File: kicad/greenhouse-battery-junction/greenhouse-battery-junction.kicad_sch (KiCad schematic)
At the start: 8 parts, among them J1 Conn_01x10_Female, J10 Conn_01x03_Female, J11 Screw_Terminal_01x02, J12 Conn_01x04_Male, J13 Screw_Terminal_01x02, J2 Conn_01x03_Female

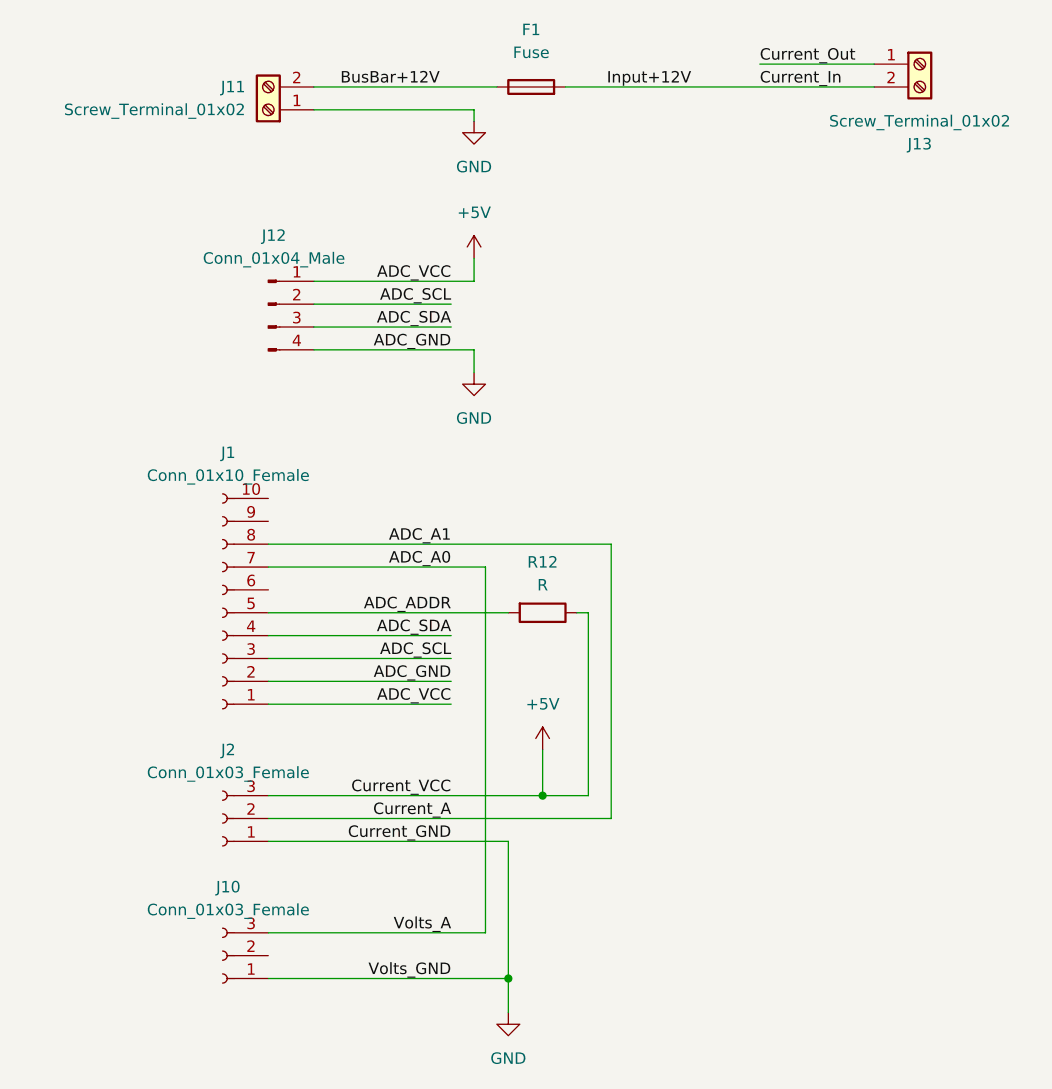
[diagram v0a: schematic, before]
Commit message: Fixed errors in battery junction
Didn't match up with prototype
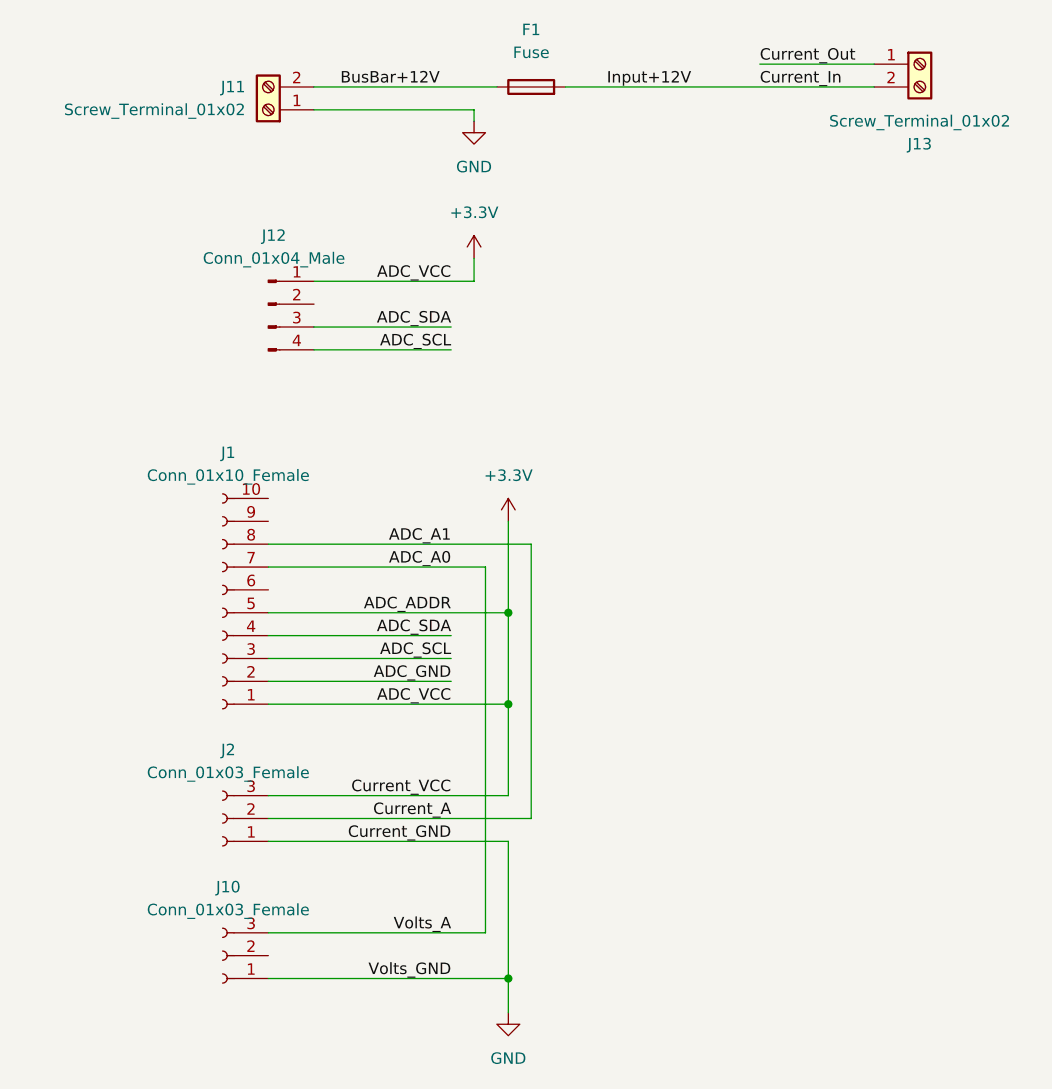
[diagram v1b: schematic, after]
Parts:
- removed R12: R, Resistor_THT:R_Box_L8.4mm_W2.5mm_P5.08mm, symbol Device:R
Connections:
- net ADC_ADDR is gone; now on net +3V3: J1.5 (Pin_5)
- net ADC_SCL: now also J12.4 (Pin_4); no longer J12.2 (Pin_2)
- net GND: no longer J1.2 (Pin_2), J12.4 (Pin_4)
- net +5V renamed +3V3
- new net ADC_GND: J1.2 (Pin_2)
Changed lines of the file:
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@@
 (kicad_sch (version 20211123) (generator eeschema)
   (paper "A4")
+  (junction (at 82.55 93.98) (diameter 0) (color 0 0 0 0)
+  )
+  (junction (at 82.55 104.14) (diameter 0) (color 0 0 0 0)
+  )
   (junction (at 82.55 134.62) (diameter 0) (color 0 0 0 0)
   )
-  (junction (at 86.36 114.3) (diameter 0) (color 0 0 0 0)
+  (wire (pts (xy 60.96 62.23) (xy 76.2 62.23))
+    (stroke (width 0) (type default) (color 0 0 0 0))
   )
   (wire (pts (xy 82.55 134.62) (xy 82.55 138.43))
     (stroke (width 0) (type default) (color 0 0 0 0))
   )
-  (wire (pts (xy 55.88 114.3) (xy 86.36 114.3))
-    (stroke (width 0) (type default) (color 0 0 0 0))
-  )
-  (wire (pts (xy 91.44 93.98) (xy 91.44 114.3))
-    (stroke (width 0) (type default) (color 0 0 0 0))
-  )
-  (wire (pts (xy 60.96 62.23) (xy 76.2 62.23))
-    (stroke (width 0) (type default) (color 0 0 0 0))
-  )
-  (wire (pts (xy 60.96 59.69) (xy 76.2 59.69))
+  (wire (pts (xy 55.88 114.3) (xy 82.55 114.3))
     (stroke (width 0) (type default) (color 0 0 0 0))
   )
@@
     (stroke (width 0) (type default) (color 0 0 0 0))
   )
+  (wire (pts (xy 82.55 93.98) (xy 82.55 104.14))
+    (stroke (width 0) (type default) (color 0 0 0 0))
+  )
   (wire (pts (xy 55.88 119.38) (xy 82.55 119.38))
     (stroke (width 0) (type default) (color 0 0 0 0))
   )
-  (wire (pts (xy 55.88 86.36) (xy 93.98 86.36))
+  (wire (pts (xy 60.96 64.77) (xy 76.2 64.77))
+    (stroke (width 0) (type default) (color 0 0 0 0))
+  )
+  (wire (pts (xy 55.88 86.36) (xy 85.09 86.36))
+    (stroke (width 0) (type default) (color 0 0 0 0))
+  )
+  (wire (pts (xy 82.55 104.14) (xy 82.55 114.3))
     (stroke (width 0) (type default) (color 0 0 0 0))
   )
@@
     (stroke (width 0) (type default) (color 0 0 0 0))
   )
-  (wire (pts (xy 93.98 86.36) (xy 93.98 116.84))
-    (stroke (width 0) (type default) (color 0 0 0 0))
-  )
-  (wire (pts (xy 86.36 114.3) (xy 91.44 114.3))
-    (stroke (width 0) (type default) (color 0 0 0 0))
-  )
-  (wire (pts (xy 55.88 116.84) (xy 93.98 116.84))
-    (stroke (width 0) (type default) (color 0 0 0 0))
-  )
-  (wire (pts (xy 78.74 67.31) (xy 78.74 64.77))
-    (stroke (width 0) (type default) (color 0 0 0 0))
-  )
-  (wire (pts (xy 90.17 93.98) (xy 91.44 93.98))
+  (wire (pts (xy 85.09 86.36) (xy 85.09 116.84))
+    (stroke (width 0) (type default) (color 0 0 0 0))
+  )
+  (wire (pts (xy 55.88 116.84) (xy 85.09 116.84))
+    (stroke (width 0) (type default) (color 0 0 0 0))
+  )
+  (wire (pts (xy 55.88 104.14) (xy 82.55 104.14))
     (stroke (width 0) (type default) (color 0 0 0 0))
   )
@@
     (stroke (width 0) (type default) (color 0 0 0 0))
   )
-  (wire (pts (xy 55.88 104.14) (xy 76.2 104.14))
-    (stroke (width 0) (type default) (color 0 0 0 0))
-  )
   (wire (pts (xy 80.01 88.9) (xy 80.01 129.54))
     (stroke (width 0) (type default) (color 0 0 0 0))
@@
     (stroke (width 0) (type default) (color 0 0 0 0))
   )
-  (wire (pts (xy 86.36 109.22) (xy 86.36 114.3))
-    (stroke (width 0) (type default) (color 0 0 0 0))
-  )
   (wire (pts (xy 82.55 134.62) (xy 82.55 119.38))
     (stroke (width 0) (type default) (color 0 0 0 0))
@@
     (stroke (width 0) (type default) (color 0 0 0 0))
   )
-  (wire (pts (xy 60.96 64.77) (xy 78.74 64.77))
-    (stroke (width 0) (type default) (color 0 0 0 0))
-  )
   (wire (pts (xy 55.88 88.9) (xy 80.01 88.9))
     (stroke (width 0) (type default) (color 0 0 0 0))
@@
     (stroke (width 0) (type default) (color 0 0 0 0))
   )
+  (wire (pts (xy 82.55 83.82) (xy 82.55 93.98))
+    (stroke (width 0) (type default) (color 0 0 0 0))
+  )
   (wire (pts (xy 88.9 35.56) (xy 123.19 35.56))
     (stroke (width 0) (type default) (color 0 0 0 0))
@@
     (effects (font (size 1.27 1.27)) (justify right bottom))
   )
-  (label "ADC_SDA" (at 76.2 62.23 180)
-    (effects (font (size 1.27 1.27)) (justify right bottom))
-  )
   (label "Current_GND" (at 76.2 119.38 180)
     (effects (font (size 1.27 1.27)) (justify right bottom))
@@
     (effects (font (size 1.27 1.27)) (justify right bottom))
   )
+  (label "ADC_SCL" (at 76.2 64.77 180)
+    (effects (font (size 1.27 1.27)) (justify right bottom))
+  )
   (label "ADC_A1" (at 76.2 86.36 180)
     (effects (font (size 1.27 1.27)) (justify right bottom))
   )
   (label "ADC_VCC" (at 76.2 104.14 180)
-    (effects (font (size 1.27 1.27)) (justify right bottom))
-  )
-  (label "ADC_GND" (at 76.2 64.77 180)
     (effects (font (size 1.27 1.27)) (justify right bottom))
   )
@@
     (effects (font (size 1.27 1.27)) (justify left bottom))
   )
+  (label "ADC_SDA" (at 76.2 62.23 180)
+    (effects (font (size 1.27 1.27)) (justify right bottom))
+  )
   (label "Current_A" (at 76.2 116.84 180)
     (effects (font (size 1.27 1.27)) (justify right bottom))
@@
     (effects (font (size 1.27 1.27)) (justify right bottom))
   )
-  (label "ADC_SCL" (at 76.2 59.69 180)
-    (effects (font (size 1.27 1.27)) (justify right bottom))
-  )
   (label "ADC_VCC" (at 76.2 57.15 180)
     (effects (font (size 1.27 1.27)) (justify right bottom))
-  )
-  (symbol (lib_id "Device:R") (at 86.36 93.98 270) (unit 1)
-    (in_bom yes) (on_board yes) (fields_autoplaced)
-    (property "Reference" "R12" (id 0) (at 86.36 87.63 90)
-      (effects (font (size 1.27 1.27)) (justify top))
-    )
-    (property "Value" "R" (id 1) (at 86.36 90.17 90)
-      (effects (font (size 1.27 1.27)) (justify top))
-    )
-    (property "Footprint" "Resistor_THT:R_Box_L8.4mm_W2.5mm_P5.08mm" (id 2) (at 86.36 92.202 90)
-      (effects (font (size 1.27 1.27)) hide)
-    )
-    (property "Datasheet" "~" (id 3) (at 86.36 93.98 0)
-      (effects (font (size 1.27 1.27)) hide)
-    )
-    (pin "1")
-    (pin "2")
   )
   (symbol (lib_id "power:GND") (at 82.55 138.43 0) (unit 1)
@@
     (pin "2")
   )
-  (symbol (lib_id "power:+5V") (at 86.36 109.22 0) (unit 1)
-    (in_bom yes) (on_board yes) (fields_autoplaced)
-    (property "Reference" "#PWR0133" (id 0) (at 86.36 113.03 0)
-      (effects (font (size 1.27 1.27)) hide)
-    )
-    (property "Value" "+5V" (id 1) (at 86.36 104.14 0))
-    (property "Footprint" "" (id 2) (at 86.36 109.22 0)
-      (effects (font (size 1.27 1.27)) hide)
-    )
-    (property "Datasheet" "" (id 3) (at 86.36 109.22 0)
+  (symbol (lib_id "power:+3.3V") (at 82.55 83.82 0) (unit 1)
+    (in_bom yes) (on_board yes) (fields_autoplaced)
+    (property "Reference" "#PWR?" (id 0) (at 82.55 87.63 0)
+      (effects (font (size 1.27 1.27)) hide)
+    )
+    (property "Value" "+3.3V" (id 1) (at 82.55 78.74 0))
+    (property "Footprint" "" (id 2) (at 82.55 83.82 0)
+      (effects (font (size 1.27 1.27)) hide)
+    )
+    (property "Datasheet" "" (id 3) (at 82.55 83.82 0)
       (effects (font (size 1.27 1.27)) hide)
     )
@@
     (pin "2")
   )
-  (symbol (lib_id "power:+5V") (at 78.74 54.61 0) (unit 1)
-    (in_bom yes) (on_board yes) (fields_autoplaced)
-    (property "Reference" "#PWR0131" (id 0) (at 78.74 58.42 0)
-      (effects (font (size 1.27 1.27)) hide)
-    )
-    (property "Value" "+5V" (id 1) (at 78.74 49.53 0))
-    (property "Footprint" "" (id 2) (at 78.74 54.61 0)
-      (effects (font (size 1.27 1.27)) hide)
-    )
-    (property "Datasheet" "" (id 3) (at 78.74 54.61 0)
-      (effects (font (size 1.27 1.27)) hide)
-    )
-    (pin "1")
-  )
   (symbol (lib_id "Connector:Conn_01x03_Female") (at 50.8 116.84 180) (unit 1)
     (in_bom yes) (on_board yes) (fields_autoplaced)
@@
     (pin "2")
   )
-  (symbol (lib_id "power:GND") (at 78.74 67.31 0) (unit 1)
-    (in_bom yes) (on_board yes) (fields_autoplaced)
-    (property "Reference" "#PWR0130" (id 0) (at 78.74 73.66 0)
-      (effects (font (size 1.27 1.27)) hide)
-    )
-    (property "Value" "GND" (id 1) (at 78.74 72.39 0))
-    (property "Footprint" "" (id 2) (at 78.74 67.31 0)
-      (effects (font (size 1.27 1.27)) hide)
-    )
-    (property "Datasheet" "" (id 3) (at 78.74 67.31 0)
-      (effects (font (size 1.27 1.27)) hide)
-    )
-    (pin "1")
-  )
   (symbol (lib_id "power:GND") (at 78.74 39.37 0) (unit 1)
     (in_bom yes) (on_board yes) (fields_autoplaced)
@@
     )
     (property "Datasheet" "" (id 3) (at 78.74 39.37 0)
+      (effects (font (size 1.27 1.27)) hide)
+    )
+    (pin "1")
+  )
+  (symbol (lib_id "power:+3.3V") (at 78.74 54.61 0) (unit 1)
+    (in_bom yes) (on_board yes) (fields_autoplaced)
+    (property "Reference" "#PWR?" (id 0) (at 78.74 58.42 0)
+      (effects (font (size 1.27 1.27)) hide)
+    )
+    (property "Value" "+3.3V" (id 1) (at 78.74 49.53 0))
+    (property "Footprint" "" (id 2) (at 78.74 54.61 0)
+      (effects (font (size 1.27 1.27)) hide)
+    )
+    (property "Datasheet" "" (id 3) (at 78.74 54.61 0)
       (effects (font (size 1.27 1.27)) hide)
     )
@@
       (reference "#PWR0129") (unit 1) (value "GND") (footprint "")
     )
-    (path "/b8da1639-6b43-4d62-aed0-d1ebbf30e691"
-      (reference "#PWR0130") (unit 1) (value "GND") (footprint "")
-    )
-    (path "/84ba6c0c-48c3-464d-bd3c-8b99d15645a2"
-      (reference "#PWR0131") (unit 1) (value "+5V") (footprint "")
-    )
     (path "/0a75bfd8-1b13-490c-81b0-96bb14fdc894"
       (reference "#PWR0132") (unit 1) (value "GND") (footprint "")
     )
-    (path "/5468b90c-8daf-4ad1-84ba-f18465be537f"
-      (reference "#PWR0133") (unit 1) (value "+5V") (footprint "")
+    (path "/6ea06f35-328b-4023-b0c8-577506471241"
+      (reference "#PWR?") (unit 1) (value "+3.3V") (footprint "")
+    )
+    (path "/e69906cd-1084-40b8-bc4a-8f253ac53ca8"
+      (reference "#PWR?") (unit 1) (value "+3.3V") (footprint "")
     )
     (path "/77776d86-79c7-4560-b80f-57ff97b9092a"
@@
       (reference "J13") (unit 1) (value "Screw_Terminal_01x02") (footprint "TerminalBlock_Phoenix:TerminalBlock_Phoenix_MKDS-1,5-2-5.08_1x02_P5.08mm_Horizontal")
     )
-    (path "/09aeed00-e816-4f55-9256-30e385af1872"
-      (reference "R12") (unit 1) (value "R") (footprint "Resistor_THT:R_Box_L8.4mm_W2.5mm_P5.08mm")
-    )
-  )
+  )
